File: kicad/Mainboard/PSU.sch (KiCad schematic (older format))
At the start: 25 parts, among them J5 BATT, J6 POT_PWR_SW, U3 LD1117S50TR_SOT223, U4 LD1117S33TR_SOT223

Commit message: Added HMC RF switch Corrected SOIC footprints assignment
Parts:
- H1, H2, H3, H4: footprint Mounting_Holes:MountingHole_2.2mm_M2_ISO14580_Pad -> MountingHole:MountingHole_2.2mm_M2_ISO14580_Pad
- U3, U4: footprint TO_SOT_Packages_SMD:SOT-223-3Lead_TabPin2 -> Package_TO_SOT_SMD:SOT-223-3_TabPin2
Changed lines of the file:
@@
 F 0 "U4" H 5450 3342 50  0000 C CNN
 F 1 "LD1117S33TR_SOT223" H 5450 3251 50  0000 C CNN
-F 2 "TO_SOT_Packages_SMD:SOT-223-3Lead_TabPin2" H 5450 3300 50  0001 C CNN
+F 2 "Package_TO_SOT_SMD:SOT-223-3_TabPin2" H 5450 3300 50  0001 C CNN
 F 3 "http://www.st.com/st-web-ui/static/active/en/resource/technical/document/datasheet/CD00000544.pdf" H 5550 2850 50  0001 C CNN
 	1    5450 3100
@@
 F 0 "H1" V 1400 6800 50  0000 L CNN
 F 1 "MountingHole_Pad" V 1500 6800 50  0000 L CNN
-F 2 "Mounting_Holes:MountingHole_2.2mm_M2_ISO14580_Pad" H 1450 6600 50  0001 C CNN
+F 2 "MountingHole:MountingHole_2.2mm_M2_ISO14580_Pad" H 1450 6600 50  0001 C CNN
 F 3 "~" H 1450 6600 50  0001 C CNN
 	1    1450 6600
@@
 F 0 "H2" V 1650 6800 50  0000 L CNN
 F 1 "MountingHole_Pad" V 1750 6800 50  0000 L CNN
-F 2 "Mounting_Holes:MountingHole_2.2mm_M2_ISO14580_Pad" H 1700 6600 50  0001 C CNN
+F 2 "MountingHole:MountingHole_2.2mm_M2_ISO14580_Pad" H 1700 6600 50  0001 C CNN
 F 3 "~" H 1700 6600 50  0001 C CNN
 	1    1700 6600
@@
 F 0 "H3" V 1900 6800 50  0000 L CNN
 F 1 "MountingHole_Pad" V 2000 6800 50  0000 L CNN
-F 2 "Mounting_Holes:MountingHole_2.2mm_M2_ISO14580_Pad" H 1950 6600 50  0001 C CNN
+F 2 "MountingHole:MountingHole_2.2mm_M2_ISO14580_Pad" H 1950 6600 50  0001 C CNN
 F 3 "~" H 1950 6600 50  0001 C CNN
 	1    1950 6600
@@
 F 0 "H4" V 2150 6800 50  0000 L CNN
 F 1 "MountingHole_Pad" V 2250 6800 50  0000 L CNN
-F 2 "Mounting_Holes:MountingHole_2.2mm_M2_ISO14580_Pad" H 2200 6600 50  0001 C CNN
+F 2 "MountingHole:MountingHole_2.2mm_M2_ISO14580_Pad" H 2200 6600 50  0001 C CNN
 F 3 "~" H 2200 6600 50  0001 C CNN
 	1    2200 6600
@@
 F 0 "U3" H 4450 3342 50  0000 C CNN
 F 1 "LD1117S50TR_SOT223" H 4450 3251 50  0000 C CNN
-F 2 "TO_SOT_Packages_SMD:SOT-223-3Lead_TabPin2" H 4450 3300 50  0001 C CNN
+F 2 "Package_TO_SOT_SMD:SOT-223-3_TabPin2" H 4450 3300 50  0001 C CNN
 F 3 "http://www.st.com/st-web-ui/static/active/en/resource/technical/document/datasheet/CD00000544.pdf" H 4550 2850 50  0001 C CNN
 	1    4450 3100

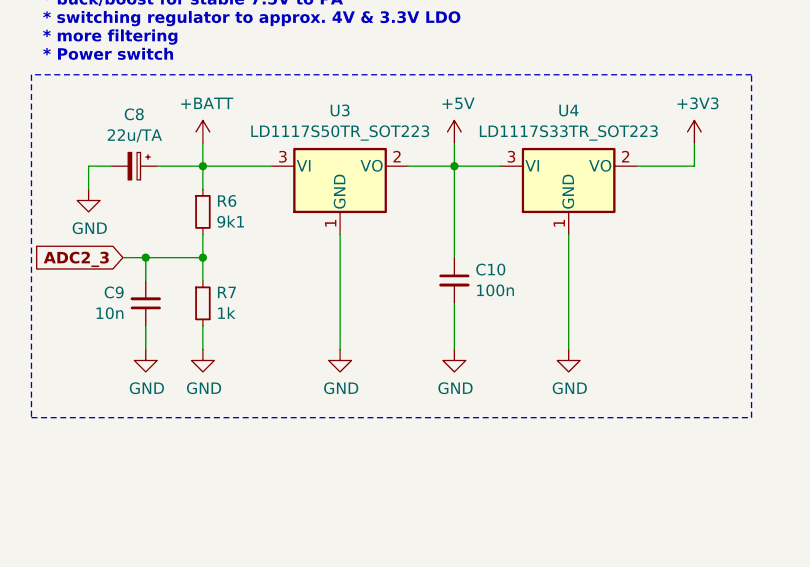
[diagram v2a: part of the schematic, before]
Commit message: started working on PCB - power supply completed plotted new PDF schematic
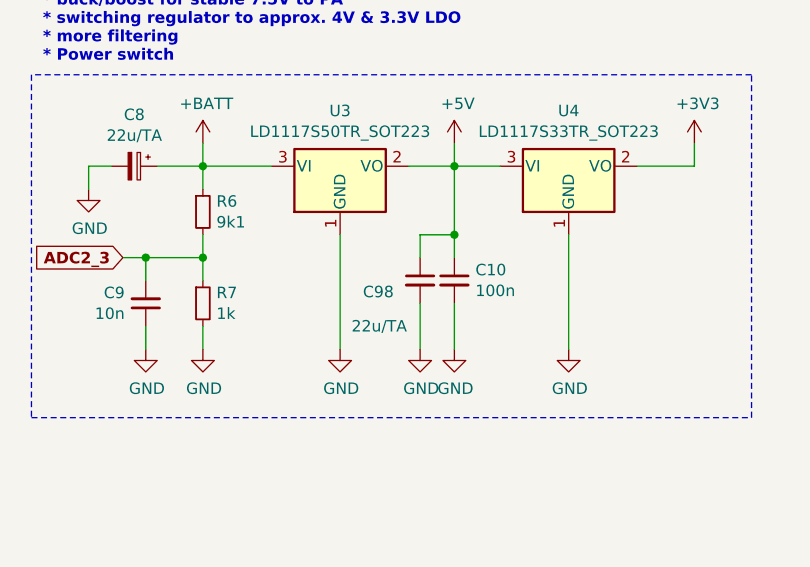
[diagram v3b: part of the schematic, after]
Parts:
- added C98: 22u/TA, Capacitor_Tantalum_SMD:CP_EIA-3216-18_Kemet-A, symbol Mainboard-rescue:C_Small-device
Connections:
- net +5V: now also C98.1
- net GND: now also C98.2
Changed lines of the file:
@@
 	4750 3100 4950 3100
 Wire Wire Line
-	4950 3100 4950 3500
+	4950 3100 4950 3400
 Connection ~ 4950 3100
 Wire Wire Line
@@
 Wire Wire Line
 	2350 3500 2500 3500
+$Comp
+L Mainboard-rescue:C_Small-device C98
+U 1 1 5E4E44F9
+P 4800 3600
+F 0 "C98" H 4550 3550 50  0000 L CNN
+F 1 "22u/TA" H 4500 3400 50  0000 L CNN
+F 2 "Capacitor_Tantalum_SMD:CP_EIA-3216-18_Kemet-A" H 4800 3600 50  0001 C CNN
+F 3 "~" H 4800 3600 50  0001 C CNN
+F 4 "TAJA226K006RNJV" H 4800 3600 50  0001 C CNN "Partno"
+	1    4800 3600
+	1    0    0    -1
+$EndComp
+Wire Wire Line
+	4800 3500 4800 3400
+Wire Wire Line
+	4800 3400 4950 3400
+Connection ~ 4950 3400
+Wire Wire Line
+	4950 3400 4950 3500
+$Comp
+L power:GND #PWR0180
+U 1 1 5E4ECAF7
+P 4800 3900
+F 0 "#PWR0180" H 4800 3650 50  0001 C CNN
+F 1 "GND" H 4805 3727 50  0000 C CNN
+F 2 "" H 4800 3900 50  0001 C CNN
+F 3 "" H 4800 3900 50  0001 C CNN
+	1    4800 3900
+	1    0    0    -1
+$EndComp
+Wire Wire Line
+	4800 3900 4800 3700
 $EndSCHEMATC

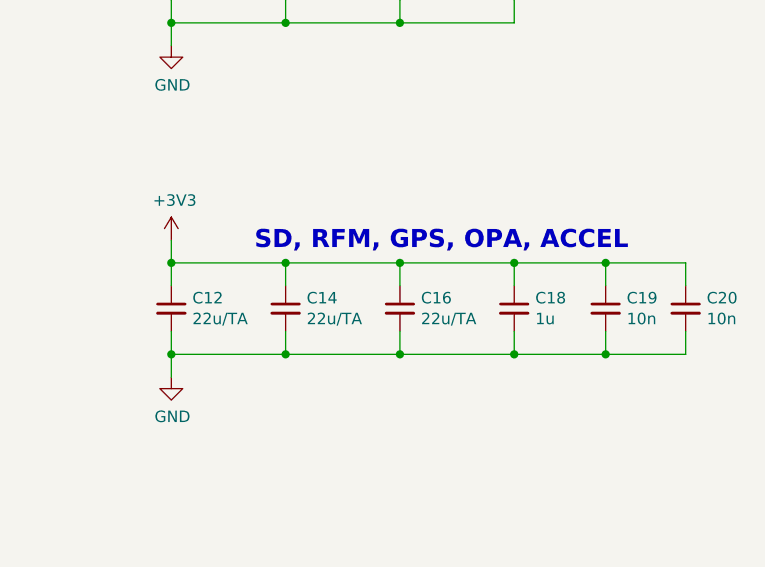
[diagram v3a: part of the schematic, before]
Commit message: added a capacitor for GPS voltage line footprints - expanded RF transistors ground plane generated new PDF added authors
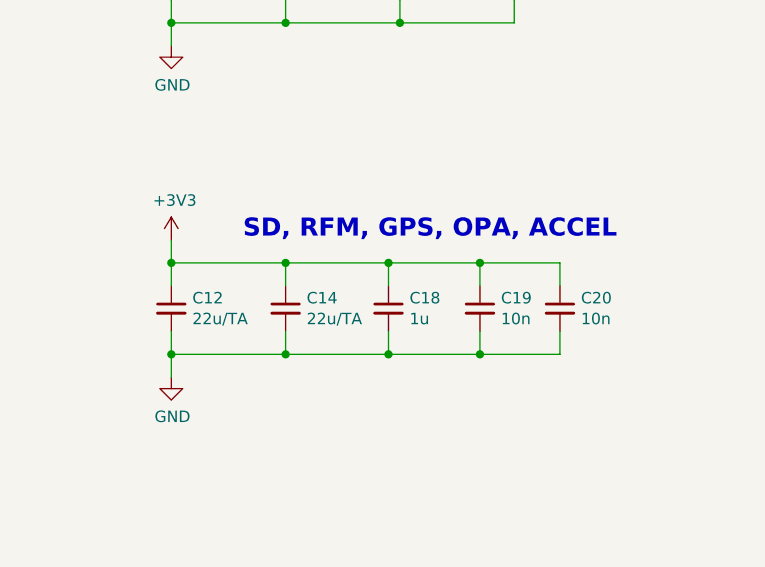
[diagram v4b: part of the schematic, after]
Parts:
- removed C16: 22u/TA, Capacitor_Tantalum_SMD:CP_EIA-3216-18_Kemet-A, symbol Mainboard-rescue:C_Small-device
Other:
- moved on the sheet: C18, C19, C20
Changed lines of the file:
@@
 Comment1 ""
 Comment2 ""
-Comment3 ""
+Comment3 "Author: DB9MAT Mathis, SO3ALG Nikoloz, SP5WWP Wojciech"
 Comment4 "TR-9 Open Source Digital Radio"
 $EndDescr
@@
 	1    0    0    -1
 $EndComp
-$Comp
-L Mainboard-rescue:C_Small-device C16
-U 1 1 5DEF7F14
-P 8650 3950
-F 0 "C16" H 8742 3996 50  0000 L CNN
-F 1 "22u/TA" H 8742 3905 50  0000 L CNN
-F 2 "Capacitor_Tantalum_SMD:CP_EIA-3216-18_Kemet-A" H 8650 3950 50  0001 C CNN
-F 3 "~" H 8650 3950 50  0001 C CNN
-F 4 "TAJA226K006RNJV" H 8650 3950 50  0001 C CNN "Partno"
-	1    8650 3950
-	1    0    0    -1
-$EndComp
 Wire Wire Line
 	8150 3750 8150 3850
@@
 	7650 3750 7650 3850
 Wire Wire Line
-	8650 3750 8650 3850
-Wire Wire Line
 	7650 4050 7650 4150
 Wire Wire Line
 	8150 4150 8150 4050
-Wire Wire Line
-	8650 4150 8650 4050
 $Comp
 L Mainboard-rescue:C_Small-device C18
 U 1 1 5DEFA72D
-P 9150 3950
-F 0 "C18" H 9242 3996 50  0000 L CNN
-F 1 "1u" H 9242 3905 50  0000 L CNN
-F 2 "Capacitor_SMD:C_0603_1608Metric" H 9150 3950 50  0001 C CNN
-F 3 "~" H 9150 3950 50  0001 C CNN
-	1    9150 3950
+P 8600 3950
+F 0 "C18" H 8692 3996 50  0000 L CNN
+F 1 "1u" H 8692 3905 50  0000 L CNN
+F 2 "Capacitor_SMD:C_0603_1608Metric" H 8600 3950 50  0001 C CNN
+F 3 "~" H 8600 3950 50  0001 C CNN
+	1    8600 3950
 	1    0    0    -1
 $EndComp
@@
 L Mainboard-rescue:C_Small-device C19
 U 1 1 5DEFAD72
-P 9550 3950
-F 0 "C19" H 9642 3996 50  0000 L CNN
-F 1 "10n" H 9642 3905 50  0000 L CNN
-F 2 "Capacitor_SMD:C_0603_1608Metric" H 9550 3950 50  0001 C CNN
-F 3 "~" H 9550 3950 50  0001 C CNN
-	1    9550 3950
+P 9000 3950
+F 0 "C19" H 9092 3996 50  0000 L CNN
+F 1 "10n" H 9092 3905 50  0000 L CNN
+F 2 "Capacitor_SMD:C_0603_1608Metric" H 9000 3950 50  0001 C CNN
+F 3 "~" H 9000 3950 50  0001 C CNN
+	1    9000 3950
 	1    0    0    -1
 $EndComp
@@
 L Mainboard-rescue:C_Small-device C20
 U 1 1 5DEFB19B
-P 9900 3950
-F 0 "C20" H 9992 3996 50  0000 L CNN
-F 1 "10n" H 9992 3905 50  0000 L CNN
-F 2 "Capacitor_SMD:C_0603_1608Metric" H 9900 3950 50  0001 C CNN
-F 3 "~" H 9900 3950 50  0001 C CNN
-	1    9900 3950
+P 9350 3950
+F 0 "C20" H 9442 3996 50  0000 L CNN
+F 1 "10n" H 9442 3905 50  0000 L CNN
+F 2 "Capacitor_SMD:C_0603_1608Metric" H 9350 3950 50  0001 C CNN
+F 3 "~" H 9350 3950 50  0001 C CNN
+	1    9350 3950
 	1    0    0    -1
 $EndComp
@@
 	7650 3750 8150 3750
 Wire Wire Line
-	8650 3750 8150 3750
-Connection ~ 8150 3750
-Wire Wire Line
-	8650 3750 9150 3750
-Wire Wire Line
-	9150 3750 9150 3850
-Connection ~ 8650 3750
-Wire Wire Line
-	9550 3750 9550 3850
-Wire Wire Line
-	9550 3750 9900 3750
-Wire Wire Line
-	9900 3750 9900 3850
-Connection ~ 9550 3750
+	8600 3750 8600 3850
+Wire Wire Line
+	9000 3750 9000 3850
+Wire Wire Line
+	9000 3750 9350 3750
+Wire Wire Line
+	9350 3750 9350 3850
+Connection ~ 9000 3750
 Wire Wire Line
 	7650 4150 8150 4150
 Wire Wire Line
-	8150 4150 8650 4150
-Connection ~ 8150 4150
-Wire Wire Line
-	9150 4050 9150 4150
-Connection ~ 8650 4150
-Wire Wire Line
-	9550 4050 9550 4150
-Wire Wire Line
-	8650 4150 9150 4150
-Wire Wire Line
-	9900 4050 9900 4150
-Wire Wire Line
-	9900 4150 9550 4150
-Connection ~ 9550 4150
-Wire Wire Line
-	9150 3750 9550 3750
-Connection ~ 9150 3750
-Wire Wire Line
-	9150 4150 9550 4150
-Connection ~ 9150 4150
+	8600 4050 8600 4150
+Wire Wire Line
+	9000 4050 9000 4150
+Wire Wire Line
+	9350 4050 9350 4150
+Wire Wire Line
+	9350 4150 9000 4150
+Connection ~ 9000 4150
+Wire Wire Line
+	8600 3750 9000 3750
+Wire Wire Line
+	8600 4150 9000 4150
 $Comp
 L power:+3V3 #PWR049
@@
 	7650 4150 7650 4250
 Connection ~ 7650 4150
-Text Notes 9650 3700 2    79   ~ 16
+Text Notes 9600 3650 2    79   ~ 16
 SD, RFM, GPS, OPA, ACCEL
 $Comp
@@
 Wire Wire Line
 	4800 3900 4800 3700
+Wire Wire Line
+	8600 3750 8150 3750
+Connection ~ 8600 3750
+Connection ~ 8150 3750
+Wire Wire Line
+	8150 4150 8600 4150
+Connection ~ 8150 4150
+Connection ~ 8600 4150
 $EndSCHEMATC

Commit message: PCB - connected microSD card to STM32 & USB frontend path routed added a schottky diode PMEG4005ET.215 footprint changed connector J7 pinout - TFT_RST swapped with UART2_RX! schootky diode added to in series to mini USB connector PDF generated
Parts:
- J5: footprint Connector_PinHeader_2.54mm:PinHeader_1x03_P2.54mm_Vertical -> Connector_PinHeader_1.27mm:PinHeader_1x03_P1.27mm_Vertical
- J6: footprint Connector_PinHeader_2.54mm:PinHeader_1x02_P2.54mm_Vertical -> Connector_PinHeader_1.27mm:PinHeader_1x02_P1.27mm_Vertical
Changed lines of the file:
@@
 F 0 "J5" H 1418 3917 50  0000 C CNN
 F 1 "BATT" H 1418 3826 50  0000 C CNN
-F 2 "Connector_PinHeader_2.54mm:PinHeader_1x03_P2.54mm_Vertical" H 1500 3600 50  0001 C CNN
+F 2 "Connector_PinHeader_1.27mm:PinHeader_1x03_P1.27mm_Vertical" H 1500 3600 50  0001 C CNN
 F 3 "~" H 1500 3600 50  0001 C CNN
 	1    1500 3600
@@
 F 0 "J6" V 2214 3062 50  0000 R CNN
 F 1 "POT_PWR_SW" V 2123 3062 50  0000 R CNN
-F 2 "Connector_PinHeader_2.54mm:PinHeader_1x02_P2.54mm_Vertical" H 2250 3250 50  0001 C CNN
+F 2 "Connector_PinHeader_1.27mm:PinHeader_1x02_P1.27mm_Vertical" H 2250 3250 50  0001 C CNN
 F 3 "~" H 2250 3250 50  0001 C CNN
 	1    2250 3250

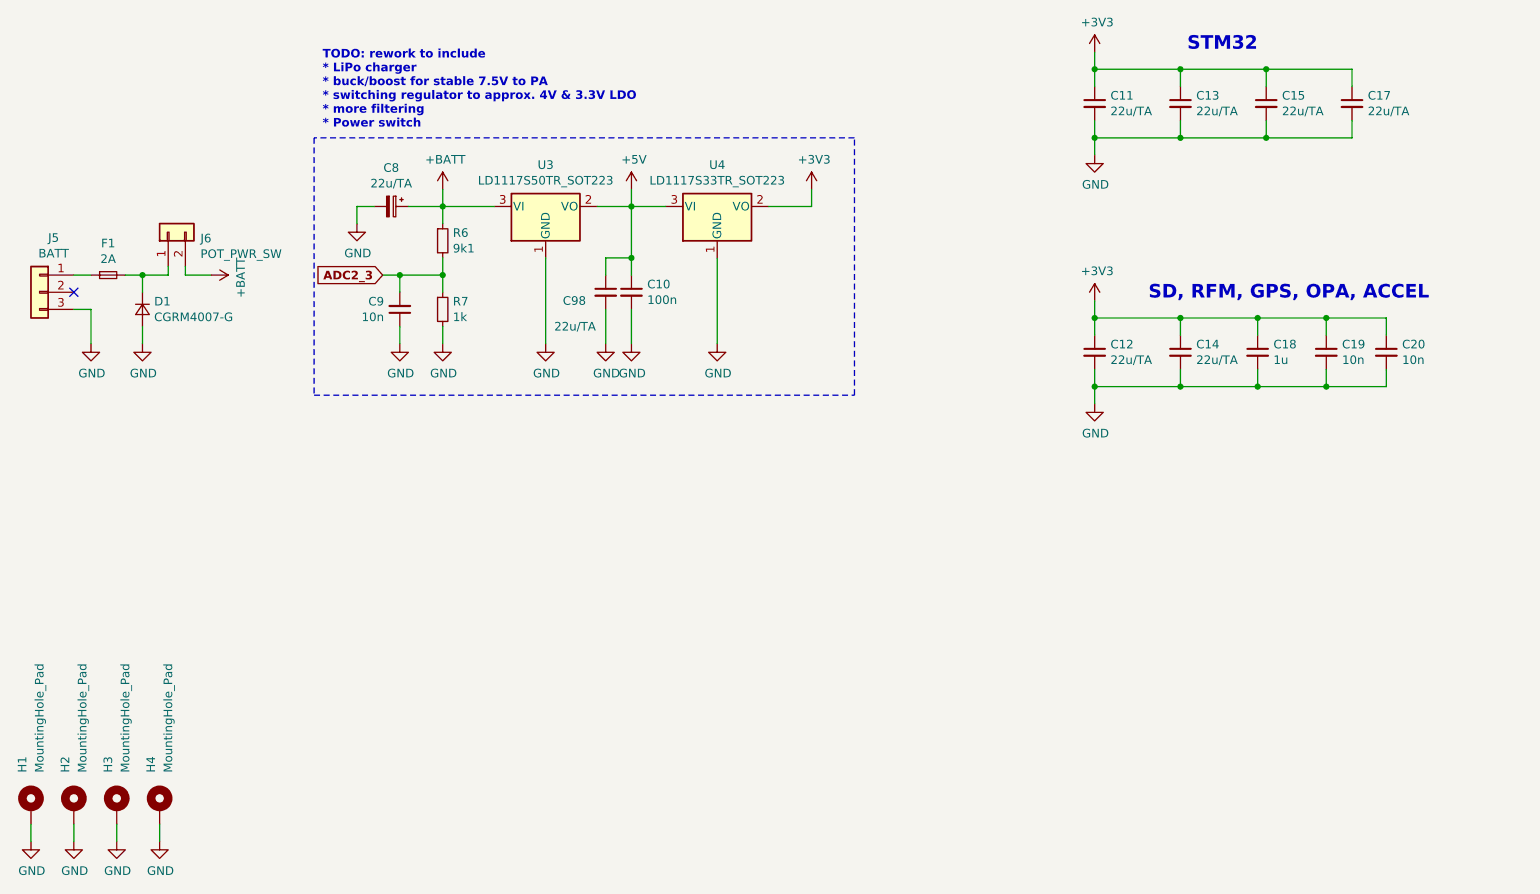
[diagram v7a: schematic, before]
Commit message: added some decoupling caps, pull ups/downs
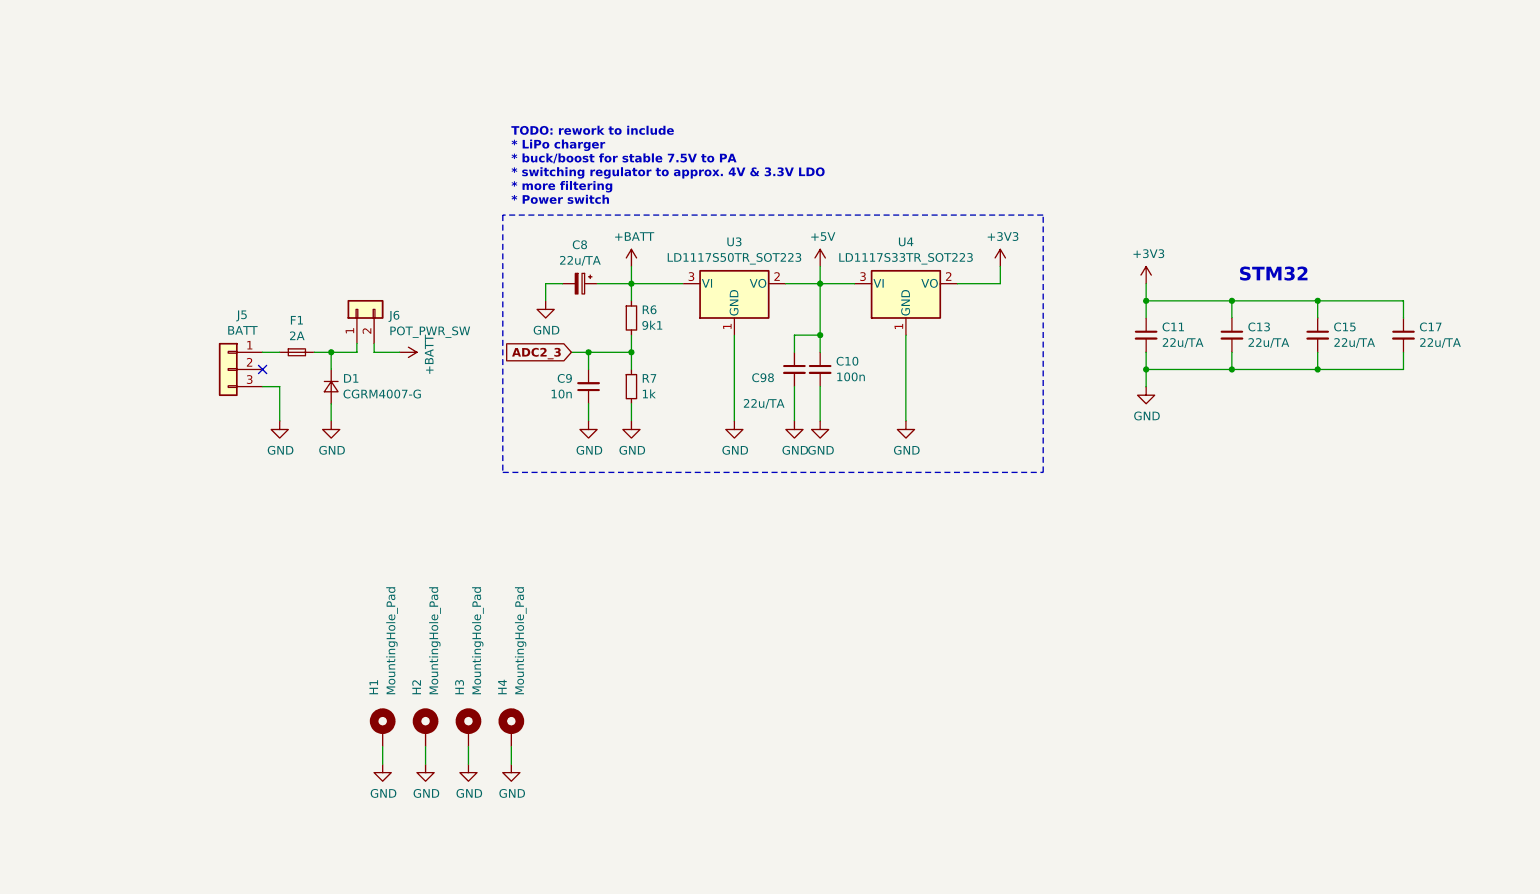
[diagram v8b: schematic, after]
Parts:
- removed C12, C14: 22u/TA, Capacitor_Tantalum_SMD:CP_EIA-3216-18_Kemet-A, symbol Mainboard-rescue:C_Small-device
- removed C18: 1u, Capacitor_SMD:C_0603_1608Metric, symbol Mainboard-rescue:C_Small-device
- removed C19, C20: 10n, Capacitor_SMD:C_0603_1608Metric, symbol Mainboard-rescue:C_Small-device
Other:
- note removed: "SD, RFM, GPS, OPA, ACCEL"
- moved on the sheet: C10, C11, C13, C15, C17, C8, C9, C98, D1, F1, H1, H2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
